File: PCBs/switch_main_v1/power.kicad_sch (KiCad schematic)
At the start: 3 parts, among them U401 LT8692SIV-PBF, U402 TPS16416DRCR, U403 LMR34206SC5QRNXRQ1

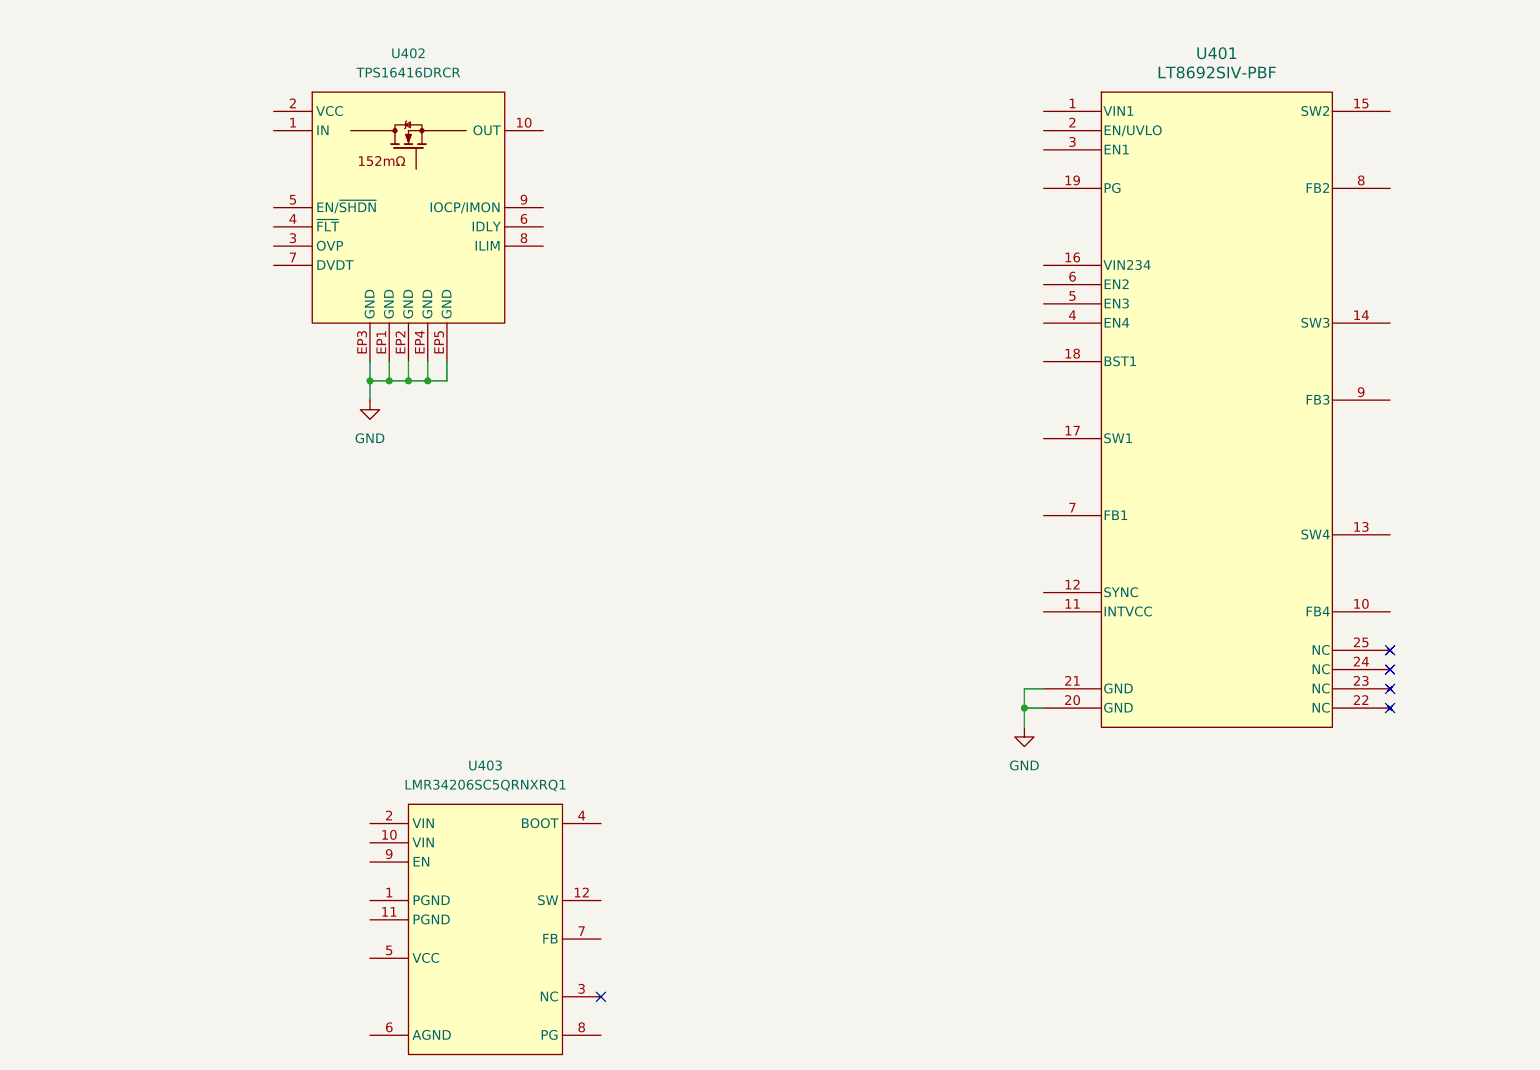
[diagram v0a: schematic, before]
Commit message: Connectors schematic almost complete
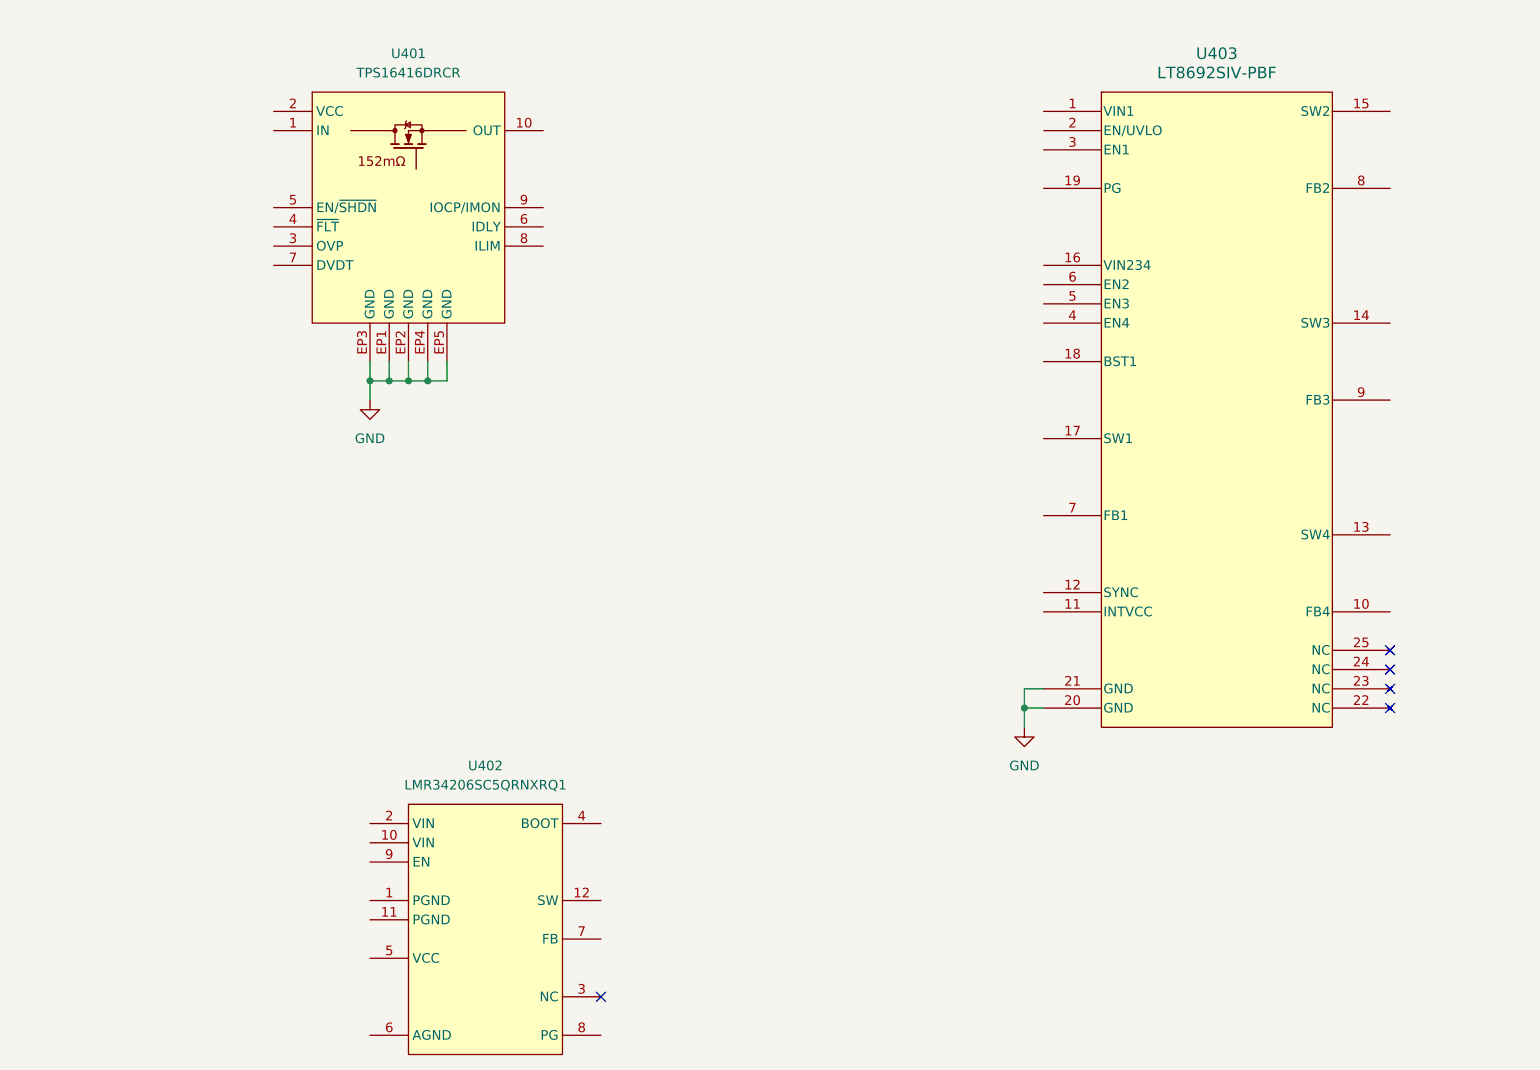
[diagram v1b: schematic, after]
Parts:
- renumbered U402 to U401, U403 to U402, U401 to U403
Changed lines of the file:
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@@
 		(dnp no)
 		(fields_autoplaced yes)
-		(property "Reference" "U401"
+		(property "Reference" "U403"
 			(at 187.96 35.56 0)
 			(effects
@@
 			(project "switch_main_v1"
 				(path "/4638d344-96ef-43ce-a37a-2df37185796e/ef57f6d4-7976-4470-9a64-870882b874ba"
-					(reference "U401")
+					(reference "U403")
 					(unit 1)
 				)
@@
 		(dnp no)
 		(fields_autoplaced yes)
-		(property "Reference" "U402"
+		(property "Reference" "U401"
 			(at 81.28 35.56 0)
 			(effects
@@
 			(project "switch_main_v1"
 				(path "/4638d344-96ef-43ce-a37a-2df37185796e/ef57f6d4-7976-4470-9a64-870882b874ba"
-					(reference "U402")
+					(reference "U401")
 					(unit 1)
 				)
@@
 		(dnp no)
 		(fields_autoplaced yes)
-		(property "Reference" "U403"
+		(property "Reference" "U402"
 			(at 91.44 129.54 0)
 			(effects
@@
 			(project "switch_main_v1"
 				(path "/4638d344-96ef-43ce-a37a-2df37185796e/ef57f6d4-7976-4470-9a64-870882b874ba"
-					(reference "U403")
+					(reference "U402")
 					(unit 1)
 				)

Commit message: Block diagram layout change
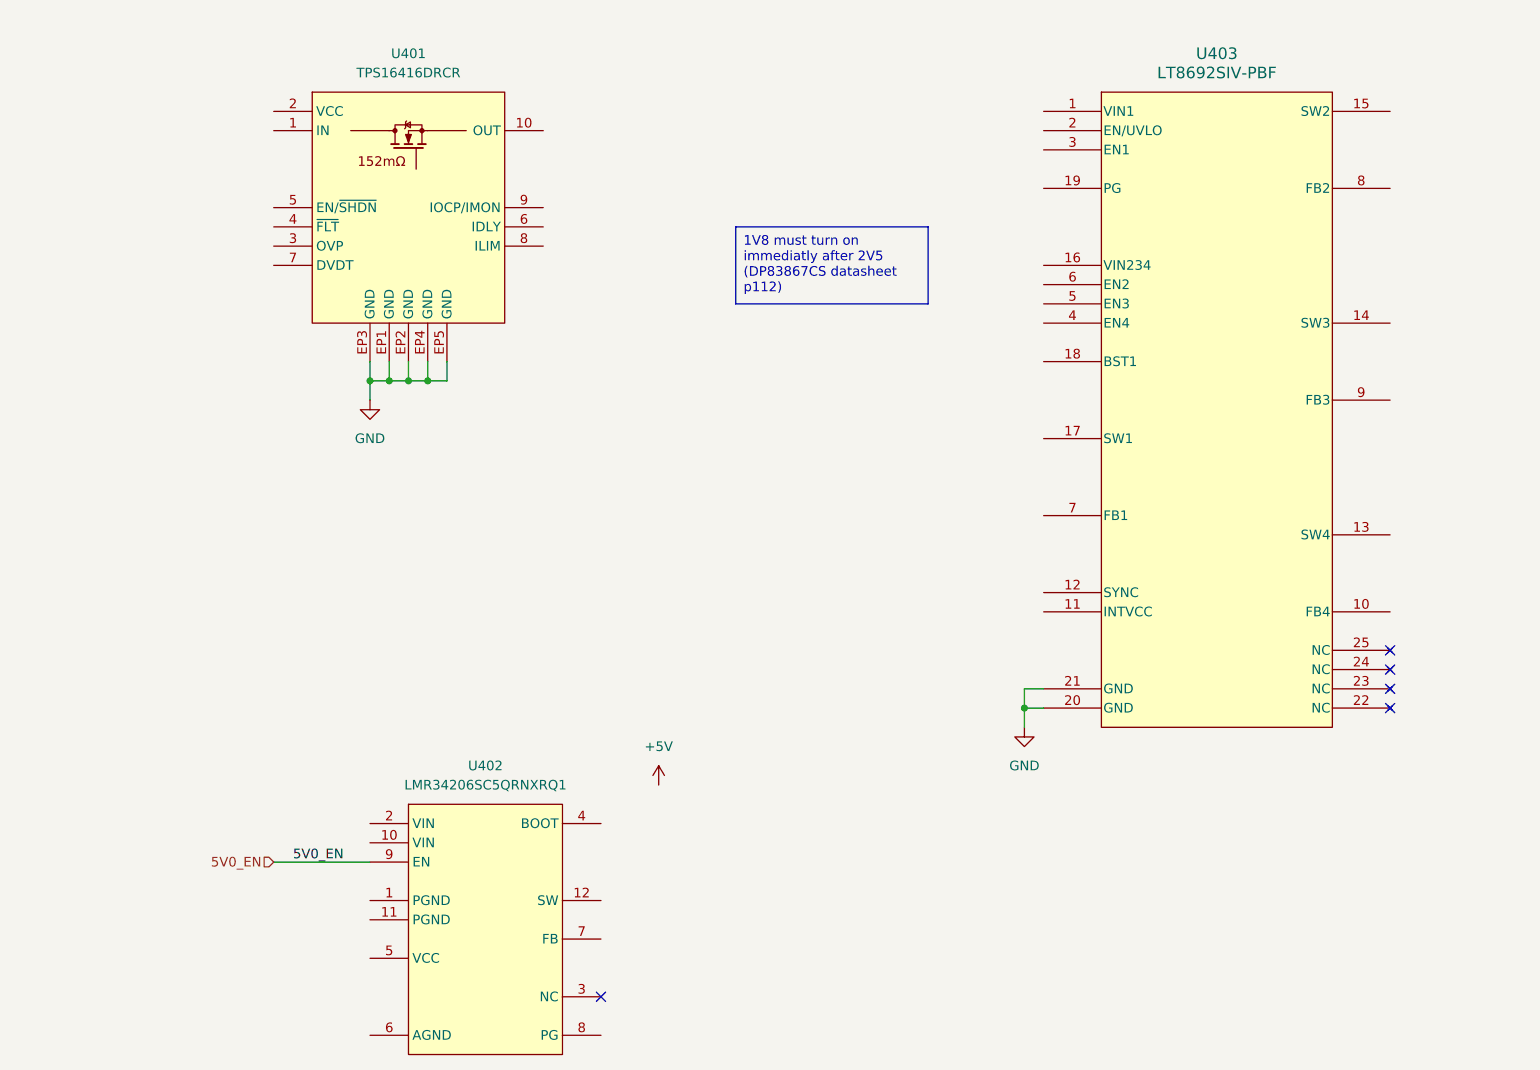
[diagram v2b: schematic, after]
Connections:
- net 5V0_EN: now reaches U402.9 (EN)
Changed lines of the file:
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@@
 	(generator_version "8.0")
 	(paper "A4")
+	(title_block
+		(date "2024-04-06")
+		(rev "0.0.0")
+	)
 	(junction
 		(at 83.82 78.74)
@@
 	(wire
 		(pts
+			(xy 63.5 142.24) (xy 76.2 142.24)
+		)
+		(stroke
+			(width 0)
+			(type default)
+		)
+	)
+	(wire
+		(pts
 			(xy 86.36 78.74) (xy 86.36 76.2)
 		)
@@
 			(width 0)
 			(type default)
+		)
+	)
+	(text_box "1V8 must turn on immediatly after 2V5\n(DP83867CS datasheet p112)"
+		(exclude_from_sim no)
+		(at 124.46 58.42 0)
+		(size 25.4 10.16)
+		(stroke
+			(width 0)
+			(type default)
+		)
+		(fill
+			(type color)
+			(color 255 229 191 1)
+		)
+		(effects
+			(font
+				(size 1.27 1.27)
+			)
+			(justify left top)
+		)
+	)
+	(label "5V0_EN"
+		(at 66.04 142.24 0)
+		(fields_autoplaced yes)
+		(effects
+			(font
+				(size 1.27 1.27)
+			)
+			(justify left bottom)
+		)
+	)
+	(hierarchical_label "5V0_EN"
+		(shape input)
+		(at 63.5 142.24 180)
+		(fields_autoplaced yes)
+		(effects
+			(font
+				(size 1.27 1.27)
+			)
+			(justify right)
 		)
 	)
@@
 					(unit 1)
 				)
+			)
+		)
+	)
+	(symbol
+		(lib_id "power:+5V")
+		(at 114.3 132.08 0)
+		(unit 1)
+		(exclude_from_sim no)
+		(in_bom yes)
+		(on_board yes)
+		(dnp no)
+		(fields_autoplaced yes)
+		(property "Reference" "#PWR0403"
+			(at 114.3 135.89 0)
+			(effects
+				(font
+					(size 1.27 1.27)
+				)
+				(hide yes)
+			)
+		)
+		(property "Value" "+5V"
+			(at 114.3 127 0)
+			(effects
+				(font
+					(size 1.27 1.27)
+				)
+			)
+		)
+		(property "Footprint" ""
+			(at 114.3 132.08 0)
+			(effects
+				(font
+					(size 1.27 1.27)
+				)
+				(hide yes)
+			)
+		)
+		(property "Datasheet" ""
+			(at 114.3 132.08 0)
+			(effects
+				(font
+					(size 1.27 1.27)
+				)
+				(hide yes)
+			)
+		)
+		(property "Description" "Power symbol creates a global label with name \"+5V\""
+			(at 114.3 132.08 0)
+			(effects
+				(font
+					(size 1.27 1.27)
+				)
+				(hide yes)
+			)
+		)
+		(pin "1"
+		)
+		(instances
+			(project "switch_main_v1"
+				(path "/4638d344-96ef-43ce-a37a-2df37185796e/ef57f6d4-7976-4470-9a64-870882b874ba"
+					(reference "#PWR0403")
+					(unit 1)
+				)

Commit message: GbE part of schematic done
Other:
- company: (none) -> Ben Smith
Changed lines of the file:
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@@
 		(date "2024-04-06")
 		(rev "0.0.0")
+		(company "Ben Smith")
 	)
 	(junction

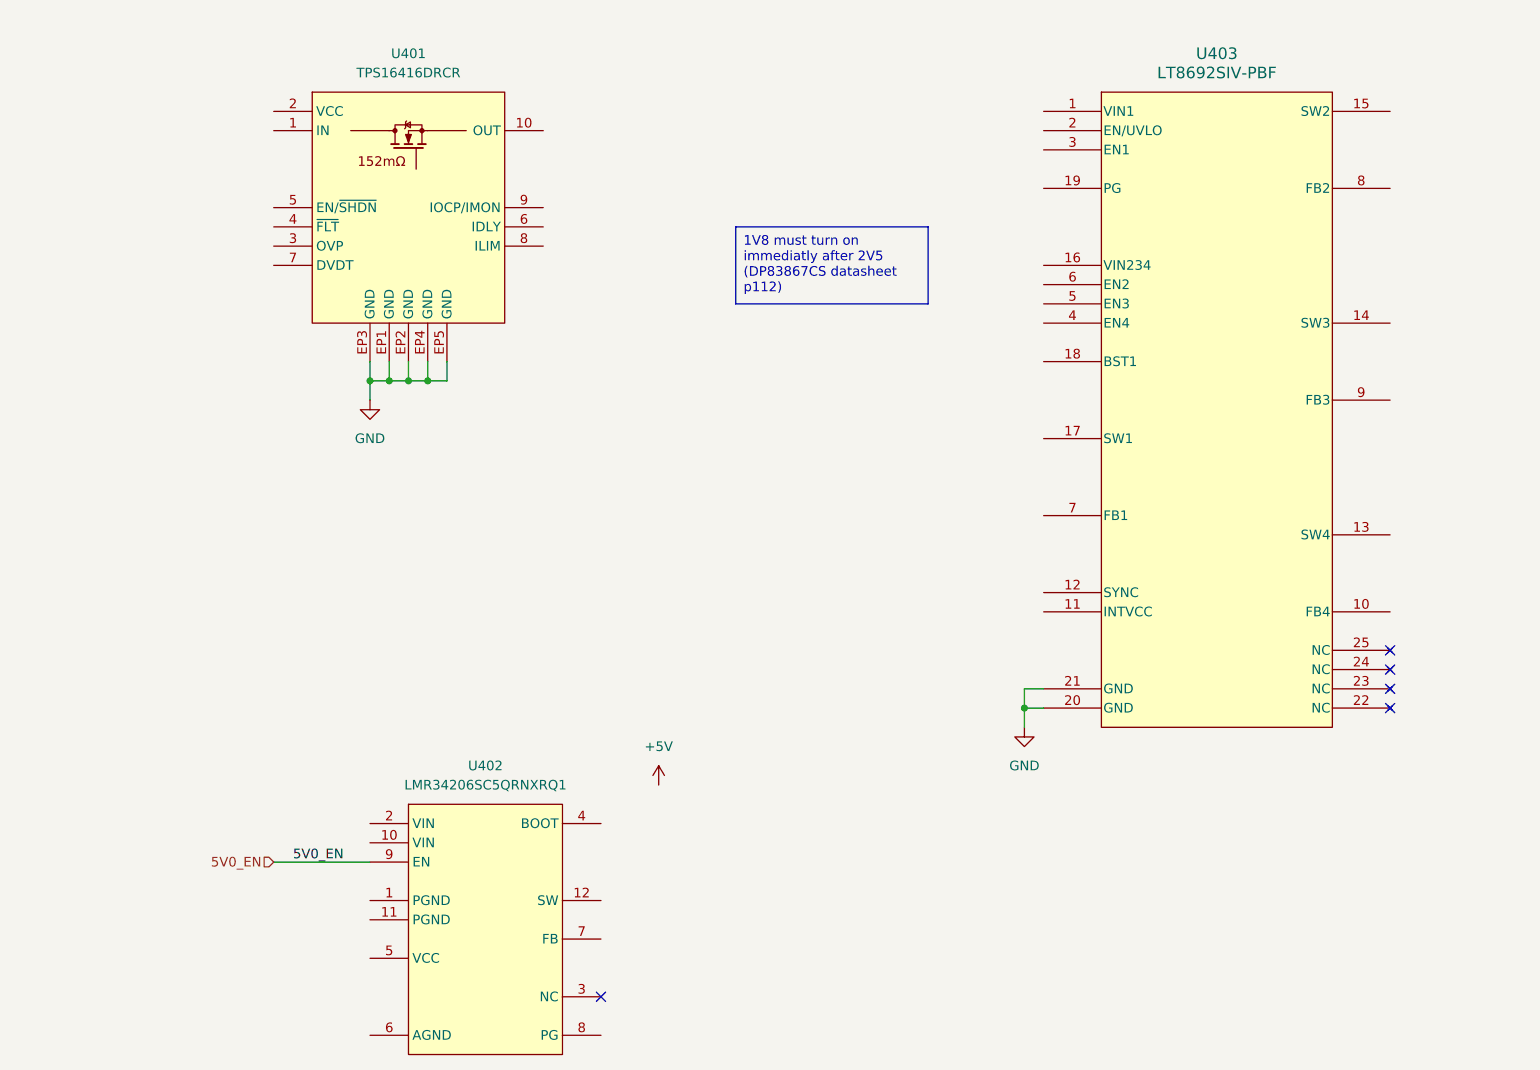
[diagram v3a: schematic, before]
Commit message: Changed MCU to STM32H573VIT3Q
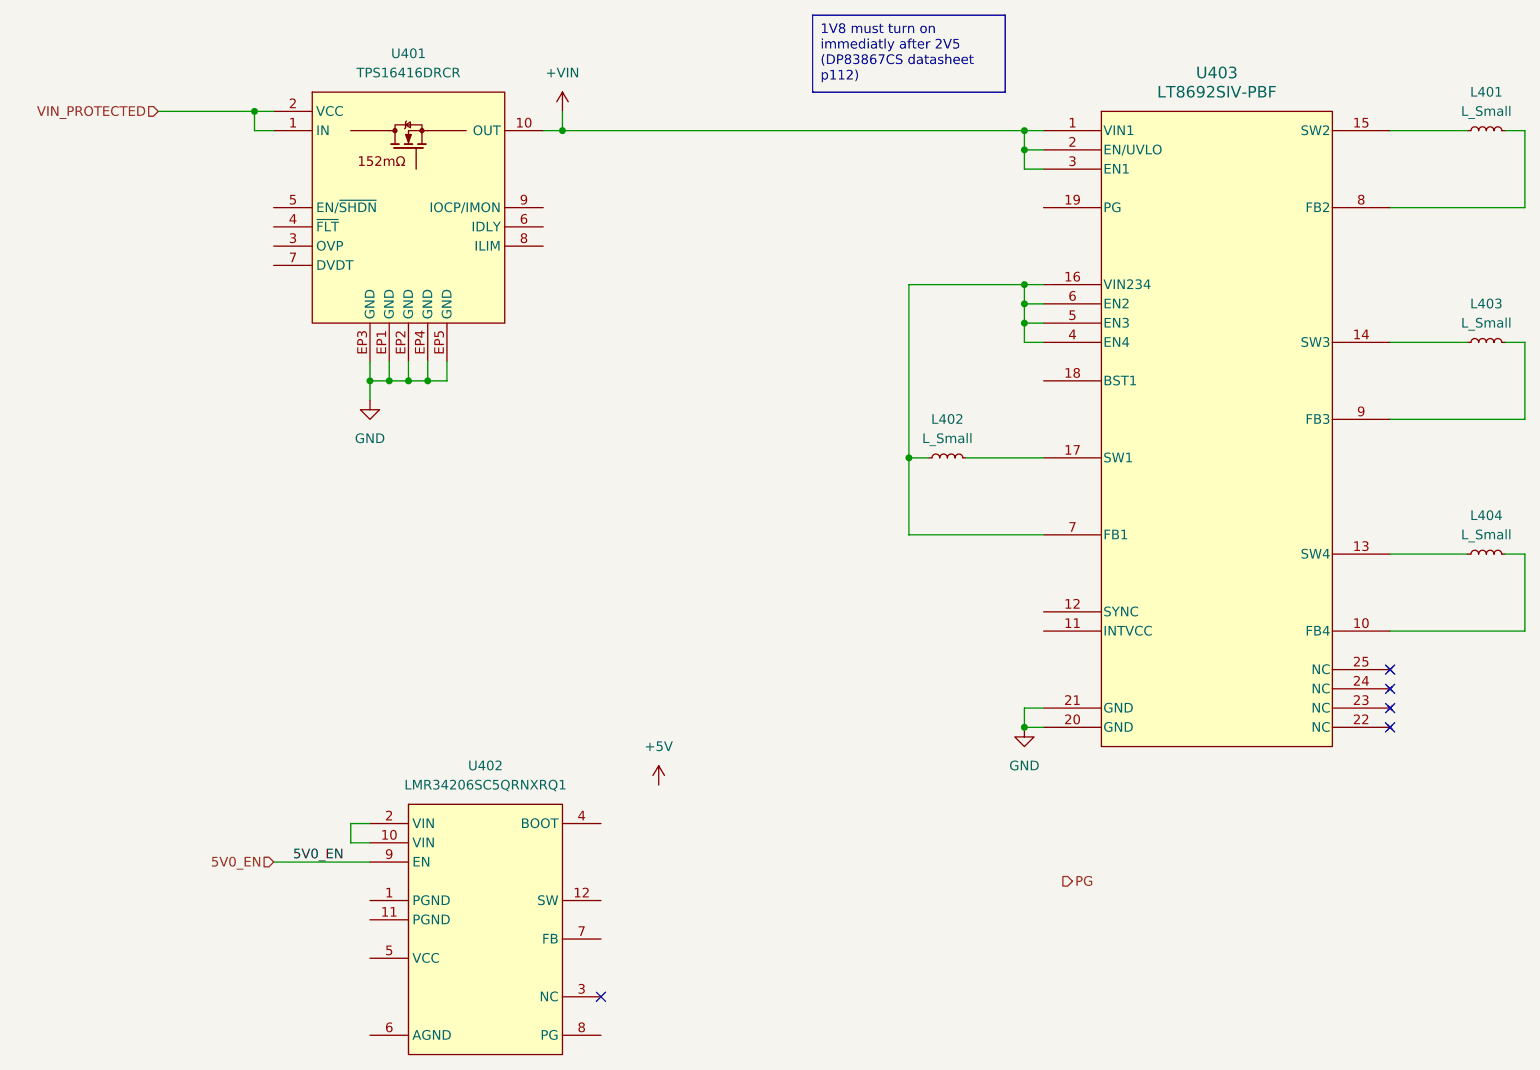
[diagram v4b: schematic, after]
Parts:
- added L401, L402, L403, L404: L_Small, symbol Device:L_Small
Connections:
- net +VIN: now reaches U403.1 (VIN1)
- net +VIN: now also U401.10 (OUT), U403.2 (EN/UVLO), U403.3 (EN1)
- net at U403.10 (FB4): now also L404.2
- net at U403.13 (SW4): now also L404.1
- net at U403.14 (SW3): now also L403.1
- net at U403.15 (SW2): now also L401.1
- net at U403.16 (VIN234): now also U403.4 (EN4), U403.5 (EN3), U403.6 (EN2), U403.7 (FB1), L402.1
- net at U403.17 (SW1): now also L402.2
- net at U403.8 (FB2): now also L401.2
- net at U403.9 (FB3): now also L403.2
- net VIN_PROTECTED: now reaches U401.1 (IN)
- net VIN_PROTECTED: now also U401.2 (VCC)
- net at U402.10 (VIN): now also U402.2 (VIN)
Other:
- moved on the sheet: U403
